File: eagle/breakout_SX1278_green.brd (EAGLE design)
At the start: 28.6 x 28.6 mm, 20 parts, among them X1 734120110

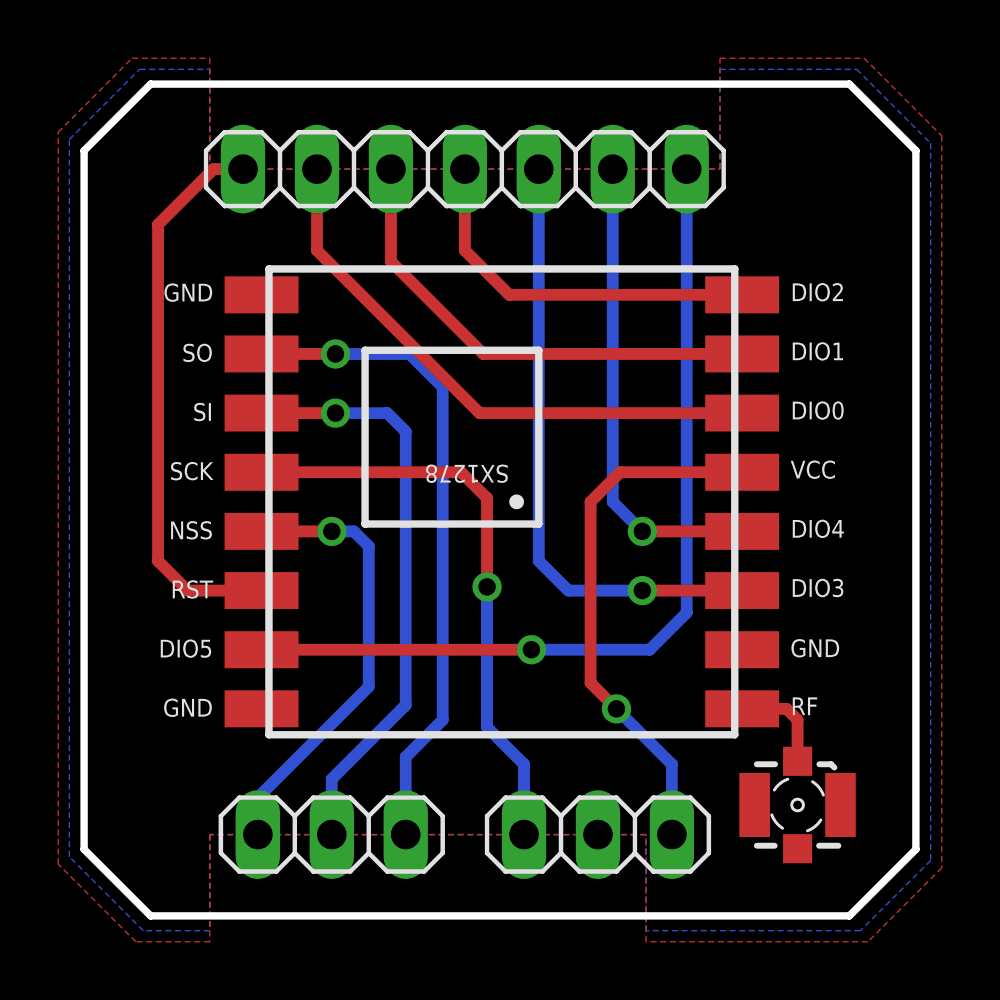
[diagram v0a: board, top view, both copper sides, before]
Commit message: Major layout update, read details
The layouts of shield and all breakout boards were changed to match the new multiprotocol standard.
IMPORTANT: The new shield is NOT compatible with the old breakout boards!
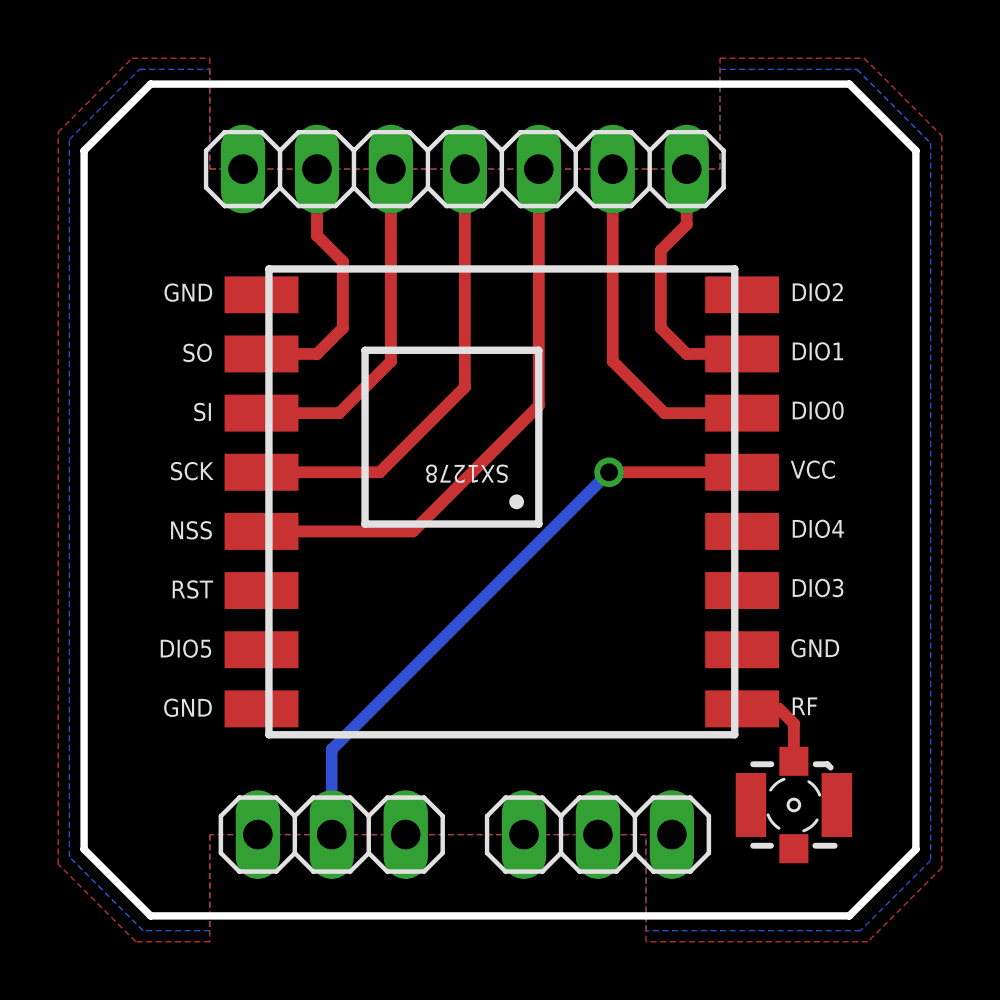
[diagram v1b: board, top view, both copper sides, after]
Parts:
- moved X1 0.13 mm to (24.4, 3.81)
- renumbered JP1 to CON_2, JP2A to CON_0, JP2B to CON_1
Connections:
- removed net 3.3V: CON_0.1, VCC.1
- removed net DIO2: CON_2.4, DIO2.1
- removed net DIO3: CON_2.5, DIO3.1
- removed net DIO4: CON_2.6, DIO4.1
- removed net DIO5: CON_2.7, DIO5.1
- removed net RESET: CON_2.1, RST.1
- new net VCC: CON_1.2, VCC.1
- net DIO0: now also CON_2.6; no longer CON_2.2
- net DIO1: now also CON_2.7; no longer CON_2.3
- net GND: now also CON_1.3; no longer CON_0.2
- net MISO: now also CON_2.2; no longer CON_1.1
- net MOSI: now also CON_2.3; no longer CON_1.2
- net NSS: now also CON_2.5; no longer CON_1.3
- net SCK: now also CON_2.4; no longer CON_0.3
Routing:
- net DIO5: track 30.4 -> 0.00 mm, vias 1 -> 0
- net VCC: track 0.00 -> 21.0 mm, vias 0 -> 1
- net DIO3: track 20.9 -> 0.00 mm, vias 1 -> 0
- net RESET: track 19.2 -> 0.00 mm
- net 3.3V: track 18.2 -> 0.00 mm, vias 1 -> 0
- net DIO4: track 16.3 -> 0.00 mm, vias 1 -> 0
- net MISO: track 22.6 -> 8.99 mm, vias 1 -> 0
- net DIO2: track 13.0 -> 0.00 mm
- net MOSI: track 20.1 -> 11.8 mm, vias 1 -> 0
- net DIO0: track 19.7 -> 11.8 mm
- net DIO1: track 16.6 -> 8.99 mm
- net SCK: track 20.2 -> 15.7 mm, vias 1 -> 0
- net NSS: track 15.4 -> 19.4 mm, vias 1 -> 0

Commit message: Fixed power connector orientation
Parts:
- flipped CON_1 to the bottom
- renumbered VCC to 3.3V
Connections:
- net VCC renamed 3.3V
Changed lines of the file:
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@@
 <wire x1="2.286" y1="28.575" x2="0" y2="26.289" width="0.254" layer="20"/>
 <text x="24.257" y="8.89" size="0.6096" layer="25">GND</text>
-<wire x1="6.35" y1="22.225" x2="22.352" y2="22.225" width="0.254" layer="21"/>
-<wire x1="22.352" y1="22.225" x2="22.352" y2="6.223" width="0.254" layer="21"/>
-<wire x1="22.352" y1="6.223" x2="6.35" y2="6.223" width="0.254" layer="21"/>
-<wire x1="6.35" y1="6.223" x2="6.35" y2="22.225" width="0.254" layer="21"/>
+<wire x1="6.35" y1="22.225" x2="22.352" y2="22.225" width="0.254" layer="51"/>
+<wire x1="22.352" y1="22.225" x2="22.352" y2="6.223" width="0.254" layer="51"/>
+<wire x1="22.352" y1="6.223" x2="6.35" y2="6.223" width="0.254" layer="51"/>
+<wire x1="6.35" y1="6.223" x2="6.35" y2="22.225" width="0.254" layer="51"/>
 <text x="4.445" y="21.717" size="0.6096" layer="25" rot="R180">GND</text>
 <circle x="14.859" y="14.224" radius="0.127" width="0.254" layer="21"/>
@@
 <wire x1="15.621" y1="13.462" x2="9.652" y2="13.462" width="0.254" layer="21"/>
 <wire x1="9.652" y1="13.462" x2="9.652" y2="19.431" width="0.254" layer="21"/>
+<wire x1="6.35" y1="6.223" x2="22.352" y2="6.223" width="0.254" layer="21"/>
+<wire x1="6.35" y1="22.225" x2="22.352" y2="22.225" width="0.254" layer="21"/>
 </plain>
 <attributes>
@@
 <attribute name="NAME" x="24.27" y="6.896" size="0.6096" layer="25"/>
 </element>
-<element name="VCC" library="wirepad" package="SMD1,27-2,54" value="" x="22.606" y="15.24" smashed="yes" rot="R270">
+<element name="3.3V" library="wirepad" package="SMD1,27-2,54" value="" x="22.606" y="15.24" smashed="yes" rot="R270">
 <attribute name="NAME" x="24.27" y="15.024" size="0.6096" layer="25"/>
 </element>
@@
 <element name="X1" library="con-coax" package="734120110" value="734120110" x="24.384" y="3.81" smashed="yes" rot="R180"/>
 <element name="GND2" library="wirepad" package="SMD1,27-2,54" value="" x="6.096" y="21.336" smashed="yes" rot="R270"/>
-<element name="CON_1" library="pinhead" package="1X03" value="" x="8.509" y="2.794" smashed="yes" rot="R180">
-<attribute name="VALUE" x="12.319" y="5.969" size="1.27" layer="27" rot="R180"/>
+<element name="CON_1" library="pinhead" package="1X03" value="" x="8.509" y="2.794" smashed="yes" rot="MR180">
+<attribute name="VALUE" x="4.699" y="5.969" size="1.27" layer="28" rot="MR180"/>
 </element>
 <element name="CON_0" library="pinhead" package="1X03" value="" x="17.653" y="2.794" smashed="yes" rot="R180">
@@
 <wire x1="24.384" y1="6.604" x2="24.384" y2="5.31" width="0.4064" layer="1"/>
 </signal>
-<signal name="VCC">
+<signal name="3.3V">
 <contactref element="CON_1" pad="2"/>
-<contactref element="VCC" pad="1"/>
+<contactref element="3.3V" pad="1"/>
 <via x="18.034" y="15.24" extent="1-16" drill="0.6096"/>
 <wire x1="18.034" y1="15.24" x2="8.509" y2="5.715" width="0.4064" layer="16"/>
+<wire x1="22.606" y1="15.24" x2="18.034" y2="15.24" width="0.4064" layer="1"/>
 <wire x1="8.509" y1="5.715" x2="8.509" y2="2.794" width="0.4064" layer="16"/>
-<wire x1="22.606" y1="15.24" x2="18.034" y2="15.24" width="0.4064" layer="1"/>
 </signal>
 </signals>
